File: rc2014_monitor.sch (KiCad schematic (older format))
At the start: 25 parts, among them J1 Z80 Bus, J2 Pro Bus, J3 USB_B_Micro, J4 M3 Mounting Hole, SW2 SW_Push, U3 74HCT541, U4 74HCT541, U5 74HCT541, U7 MAX40200AUK, U8 MAX40200AUK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

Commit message: trace cleanup
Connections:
- net labels added: CLK
- wire segments 99 -> 101
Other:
- moved on the sheet: C3, C4, C5, J4, U3, U4, U5

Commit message: use reset to clear the displays
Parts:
- added U11: 74HCT00, Package_DIP:DIP-14_W7.62mm, symbol 74xx:74HCT00
- U9: footprint Package_TO_SOT_SMD:SOT-23 -> Package_TO_SOT_SMD:SOT-23_Handsoldering
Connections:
- net labels added: CLR, RN2_2
- wire segments 101 -> 107
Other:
- note added: "Reset Monitor & Display Blank"
- note removed: "Reset Monitor"
- moved on the sheet: C10, C3, C4, C5, JP5, SW2, U3, U4, U5, U9

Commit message: Fixed some courtyard overlaps and rotary switch orientation
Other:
- moved on the sheet: C7, C8, C9, J3, U7, U8

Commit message: changes to stepper circuit, pcb layout changes
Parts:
- DISP0, DISP1, DISP2, DISP3, DISP4, DISP5: symbol rc2014_monitor-rescue:TIL311-Display_Character -> rc2014_monitor-rescue:TIL311
- renumbered C7 to C17, C9 to C7, C10 to C9, U3 to U1, U4 to U2, U5 to U3
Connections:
- net labels added: RESET, RN2_1
- net labels removed: CLR, RN2_2
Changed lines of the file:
@@
 $EndDescr
 $Comp
-L rc2014_monitor-rescue:TIL311-Display_Character DISP5
+L rc2014_monitor-rescue:TIL311 DISP5
 U 1 1 5CB4BA92
 P 2000 1500
@@
 $EndComp
 $Comp
-L rc2014_monitor-rescue:TIL311-Display_Character DISP4
+L rc2014_monitor-rescue:TIL311 DISP4
 U 1 1 5CB4CB07
 P 3550 1500
@@
 $EndComp
 $Comp
-L rc2014_monitor-rescue:TIL311-Display_Character DISP3
+L rc2014_monitor-rescue:TIL311 DISP3
 U 1 1 5CB4D9E8
 P 5100 1500
@@
 $EndComp
 $Comp
-L rc2014_monitor-rescue:TIL311-Display_Character DISP2
+L rc2014_monitor-rescue:TIL311 DISP2
 U 1 1 5CB570C9
 P 6650 1500
@@
 $EndComp
 $Comp
-L rc2014_monitor-rescue:TIL311-Display_Character DISP0
+L rc2014_monitor-rescue:TIL311 DISP0
 U 1 1 5CB570D5
 P 9800 1500
@@
 $EndComp
 $Comp
-L rc2014_monitor-rescue:TIL311-Display_Character DISP1
+L rc2014_monitor-rescue:TIL311 DISP1
 U 1 1 5CB570CF
 P 8150 1500
@@
 $EndComp
 $Comp
-L Device:C C7
+L Device:C C17
 U 1 1 5CB2CAB8
 P 4250 6350
-F 0 "C7" H 4365 6396 50  0000 L CNN
+F 0 "C17" H 4365 6396 50  0000 L CNN
 F 1 "100nF" H 4365 6305 50  0000 L CNN
 F 2 "Capacitor_SMD:C_0805_2012Metric_Pad1.15x1.40mm_HandSolder" H 4288 6200 50  0001 C CNN
@@
 	5850 7150 2350 7150
 $Sheet
-S 6250 2850 1200 800
+S 9000 2750 1200 800
 U 5CBDBC11
 F0 "LatchSelector" 50
@@
 ~RESET
 $Comp
-L Device:C C10
+L Device:C C9
 U 1 1 5CB1BEC1
 P 3850 4700
-F 0 "C10" H 3965 4746 50  0000 L CNN
+F 0 "C9" H 3965 4746 50  0000 L CNN
 F 1 "100nF" H 3965 4655 50  0000 L CNN
 F 2 "Capacitor_SMD:C_0805_2012Metric_Pad1.15x1.40mm_HandSolder" H 3888 4550 50  0001 C CNN
@@
 	6100 5300 6100 5600
 $Comp
-L 74xx:74HCT541 U3
+L 74xx:74HCT541 U1
 U 1 1 5CB94EBF
 P 6600 4800
-F 0 "U3" H 6400 5450 50  0000 C CNN
+F 0 "U1" H 6400 5450 50  0000 C CNN
 F 1 "74HCT541" H 6600 4500 50  0000 C CNN
 F 2 "Package_DIP:DIP-20_W7.62mm" H 6600 4800 50  0001 C CNN
@@
 Connection ~ 6100 5300
 $Comp
-L 74xx:74HCT541 U4
+L 74xx:74HCT541 U2
 U 1 1 5CBBA2FE
 P 8500 4800
-F 0 "U4" H 8300 5450 50  0000 C CNN
+F 0 "U2" H 8300 5450 50  0000 C CNN
 F 1 "74HCT541" H 8500 4500 50  0000 C CNN
 F 2 "Package_DIP:DIP-20_W7.62mm" H 8500 4800 50  0001 C CNN
@@
 $EndComp
 $Comp
-L 74xx:74HCT541 U5
+L 74xx:74HCT541 U3
 U 1 1 5CBBDA4F
 P 10400 4800
-F 0 "U5" H 10200 5450 50  0000 C CNN
+F 0 "U3" H 10200 5450 50  0000 C CNN
 F 1 "74HCT541" H 10400 4500 50  0000 C CNN
 F 2 "Package_DIP:DIP-20_W7.62mm" H 10400 4800 50  0001 C CNN
@@
 	3550 6600 4000 6600
 $Comp
-L Device:C C9
+L Device:C C7
 U 1 1 5CCF3BD8
 P 4000 6350
-F 0 "C9" H 4115 6396 50  0000 L CNN
+F 0 "C7" H 4115 6396 50  0000 L CNN
 F 1 "1uF" H 4115 6305 50  0000 L CNN
 F 2 "Capacitor_SMD:C_0805_2012Metric_Pad1.15x1.40mm_HandSolder" H 4038 6200 50  0001 C CNN
@@
 $Comp
 L 74xx:74HCT00 U?
-U 4 1 5CBA6ACE
+U 3 1 5CBA6ACE
 P 4650 3950
 AR Path="/5CBDBC11/5CBA6ACE" Ref="U?"  Part="4"
-AR Path="/5CBA6ACE" Ref="U11"  Part="4"
+AR Path="/5CBA6ACE" Ref="U11"  Part="3"
 F 0 "U11" H 4650 4275 50  0000 C CNN
 F 1 "74HCT00" H 4650 4184 50  0000 C CNN
@@
 F 7 "Mouser" H 2900 -1900 50  0001 C CNN "SPR"
 F 8 "https://www.mouser.com/ProductDetail/Texas-Instruments/CD74HCT00E?qs=%2Fha2pyFadui%2FKTy9HJ5lB2bvnS2yYlFmKLu9w5G%252BX5xMG4CMjJrhdg%3D%3D" H 2900 -1900 50  0001 C CNN "SPURL"
-	4    4650 3950
+	3    4650 3950
 	1    0    0    -1
 $EndComp
@@
 	4350 3950 4350 4050
 Text GLabel 4200 3650 1    50   Input ~ 0
-RN2_2
+RN2_1
 Wire Wire Line
 	4200 3650 4200 3950
@@
 Connection ~ 4200 3950
 Text GLabel 4950 3950 2    50   Output ~ 0
-CLR
+RESET
 Wire Wire Line
 	2000 2200 3550 2200
@@
 Connection ~ 4500 2500
 Wire Wire Line
-	4500 2500 5350 2500
-Wire Wire Line
 	2950 1900 2950 2500
 Connection ~ 2950 2500
 Wire Wire Line
 	2950 2500 4500 2500
-Text GLabel 5350 2700 3    50   Input ~ 0
-CLR
+Text GLabel 5350 2600 3    50   Input ~ 0
+RESET
 Wire Wire Line
 	5900 2400 4350 2400
-Wire Wire Line
-	5350 2700 5350 2500
-Connection ~ 5350 2500
-Wire Wire Line
-	5350 2500 6050 2500
 Wire Notes Line
 	5250 3300 5250 5250
 Wire Notes Line
 	2350 3300 2350 5250
+Wire Wire Line
+	4500 2500 5350 2500
+Wire Wire Line
+	5350 2600 5350 2500
+Connection ~ 5350 2500
+Wire Wire Line
+	5350 2500 6050 2500
 $EndSCHEMATC

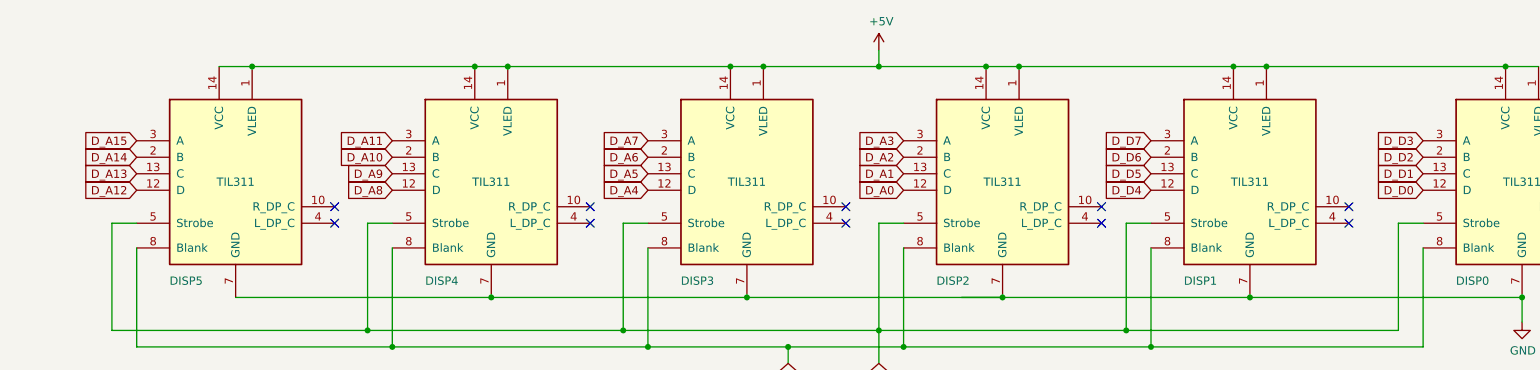
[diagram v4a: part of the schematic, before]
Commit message: fixed single step, display hookup
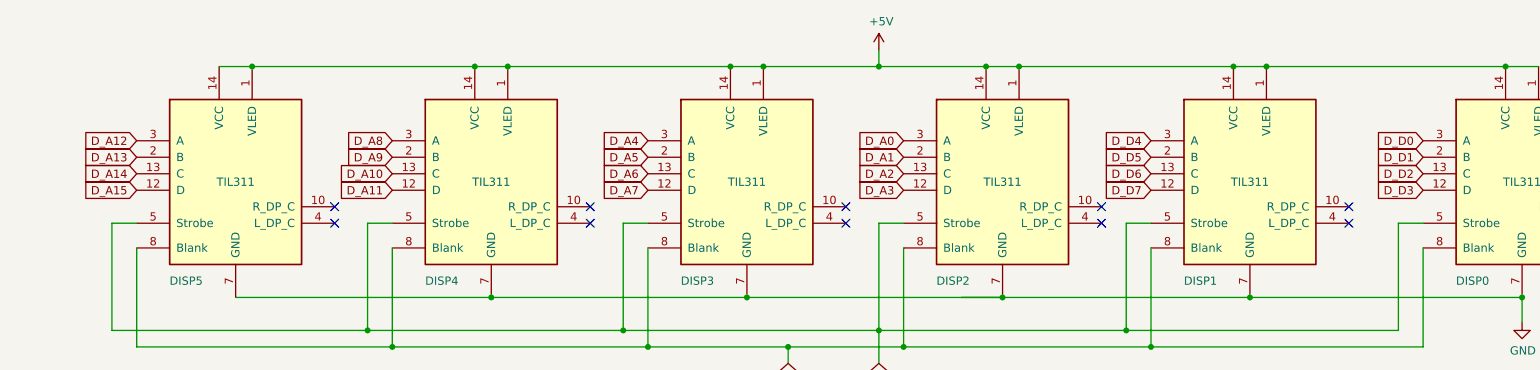
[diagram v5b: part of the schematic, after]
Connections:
- net D_A0: now also DISP2.3 (A); no longer DISP2.12 (D)
- net D_A1: now also DISP2.2 (B); no longer DISP2.13 (C)
- net D_A10: now also DISP4.13 (C); no longer DISP4.2 (B)
- net D_A11: now also DISP4.12 (D); no longer DISP4.3 (A)
- net D_A12: now also DISP5.3 (A); no longer DISP5.12 (D)
- net D_A13: now also DISP5.2 (B); no longer DISP5.13 (C)
- net D_A14: now also DISP5.13 (C); no longer DISP5.2 (B)
- net D_A15: now also DISP5.12 (D); no longer DISP5.3 (A)
- net D_A2: now also DISP2.13 (C); no longer DISP2.2 (B)
- net D_A3: now also DISP2.12 (D); no longer DISP2.3 (A)
- net D_A4: now also DISP3.3 (A); no longer DISP3.12 (D)
- net D_A5: now also DISP3.2 (B); no longer DISP3.13 (C)
- net D_A6: now also DISP3.13 (C); no longer DISP3.2 (B)
- net D_A7: now also DISP3.12 (D); no longer DISP3.3 (A)
- net D_A8: now also DISP4.3 (A); no longer DISP4.12 (D)
- net D_A9: now also DISP4.2 (B); no longer DISP4.13 (C)
- net D_D0: now also DISP0.3 (A); no longer DISP0.12 (D)
- net D_D1: now also DISP0.2 (B); no longer DISP0.13 (C)
- net D_D2: now also DISP0.13 (C); no longer DISP0.2 (B)
- net D_D3: now also DISP0.12 (D); no longer DISP0.3 (A)
- net D_D4: now also DISP1.3 (A); no longer DISP1.12 (D)
- net D_D5: now also DISP1.2 (B); no longer DISP1.13 (C)
- net D_D6: now also DISP1.13 (C); no longer DISP1.2 (B)
- net D_D7: now also DISP1.12 (D); no longer DISP1.3 (A)
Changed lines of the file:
@@
 Text GLabel 5600 6200 2    50   Input ~ 0
 5V
+Text GLabel 1400 1550 0    50   Input ~ 0
+D_A15
+Text GLabel 1400 1450 0    50   Input ~ 0
+D_A14
+Text GLabel 1400 1350 0    50   Input ~ 0
+D_A13
 Text GLabel 1400 1250 0    50   Input ~ 0
-D_A15
-Text GLabel 1400 1350 0    50   Input ~ 0
-D_A14
-Text GLabel 1400 1450 0    50   Input ~ 0
-D_A13
-Text GLabel 1400 1550 0    50   Input ~ 0
 D_A12
+Text GLabel 2950 1450 0    50   Input ~ 0
+D_A10
 Text GLabel 2950 1350 0    50   Input ~ 0
-D_A10
-Text GLabel 2950 1450 0    50   Input ~ 0
 D_A9
+Text GLabel 2950 1250 0    50   Input ~ 0
+D_A8
 Text GLabel 2950 1550 0    50   Input ~ 0
-D_A8
-Text GLabel 2950 1250 0    50   Input ~ 0
 D_A11
 Text GLabel 5900 2600 3    50   Input ~ 0
 LATCH
+Text GLabel 6050 1550 0    50   Input ~ 0
+D_A3
+Text GLabel 6050 1450 0    50   Input ~ 0
+D_A2
+Text GLabel 6050 1350 0    50   Input ~ 0
+D_A1
 Text GLabel 6050 1250 0    50   Input ~ 0
-D_A3
-Text GLabel 6050 1350 0    50   Input ~ 0
-D_A2
-Text GLabel 6050 1450 0    50   Input ~ 0
-D_A1
-Text GLabel 6050 1550 0    50   Input ~ 0
 D_A0
+Text GLabel 4500 1550 0    50   Input ~ 0
+D_A7
+Text GLabel 4500 1450 0    50   Input ~ 0
+D_A6
+Text GLabel 4500 1350 0    50   Input ~ 0
+D_A5
 Text GLabel 4500 1250 0    50   Input ~ 0
-D_A7
-Text GLabel 4500 1350 0    50   Input ~ 0
-D_A6
-Text GLabel 4500 1450 0    50   Input ~ 0
-D_A5
-Text GLabel 4500 1550 0    50   Input ~ 0
 D_A4
-Text GLabel 9200 1250 0    50   Input ~ 0
+Text GLabel 9200 1550 0    50   Input ~ 0
 D_D3
+Text GLabel 9200 1450 0    50   Input ~ 0
+D_D2
 Text GLabel 9200 1350 0    50   Input ~ 0
-D_D2
-Text GLabel 9200 1450 0    50   Input ~ 0
 D_D1
-Text GLabel 9200 1550 0    50   Input ~ 0
-D_D0
+Text GLabel 7550 1550 0    50   Input ~ 0
+D_D7
+Text GLabel 7550 1450 0    50   Input ~ 0
+D_D6
+Text GLabel 7550 1350 0    50   Input ~ 0
+D_D5
 Text GLabel 7550 1250 0    50   Input ~ 0
-D_D7
-Text GLabel 7550 1350 0    50   Input ~ 0
-D_D6
-Text GLabel 7550 1450 0    50   Input ~ 0
-D_D5
-Text GLabel 7550 1550 0    50   Input ~ 0
 D_D4
 Text GLabel 10900 4500 2    50   Output ~ 0
@@
 Wire Wire Line
 	5350 2500 6050 2500
+Text GLabel 9200 1250 0    50   Input ~ 0
+D_D0
 $EndSCHEMATC

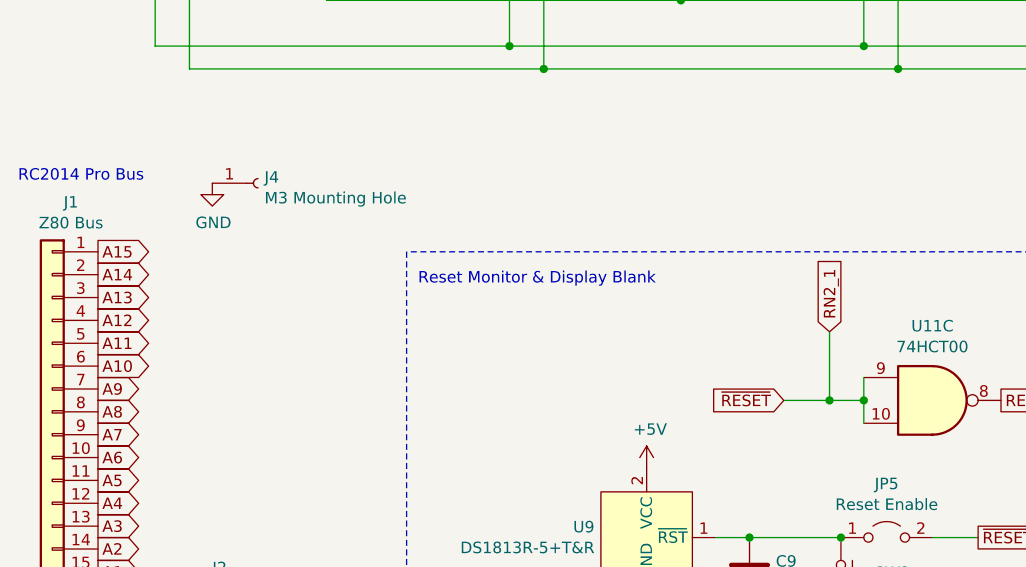
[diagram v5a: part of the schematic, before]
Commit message: Reorganized board yet again, replaced SMD 555 with TH
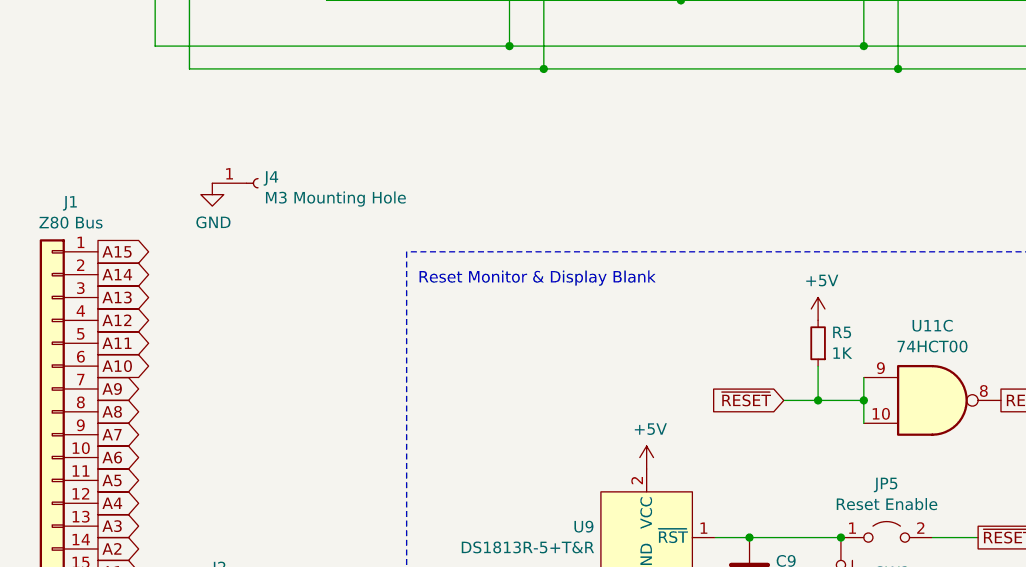
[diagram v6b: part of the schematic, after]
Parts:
- added R5: 1K, Resistor_SMD:R_0805_2012Metric_Pad1.15x1.40mm_HandSolder, symbol Device:R_Small
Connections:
- net +5V: now also R5.2
- net RN2_1 renamed ~RESET
- net ~RESET: now also R5.1
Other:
- note removed: "RC2014 Pro Bus"
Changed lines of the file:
@@
-$EndComp
-$Comp
-L power:GND #PWR0114
-U 1 1 5CB5974C
-P 2650 6900
-AR Path="/5CB5974C" Ref="#PWR0114"  Part="1"
-AR Path="/5CB63856/5CB5974C" Ref="#PWR?"  Part="1"
-AR Path="/5CB5AB00/5CB63856/5CB5974C" Ref="#PWR?"  Part="1"
-F 0 "#PWR0114" H 2650 6650 50  0001 C CNN
-F 1 "GND" H 2655 6727 50  0000 C CNN
-F 2 "" H 2650 6900 50  0001 C CNN
-F 3 "" H 2650 6900 50  0001 C CNN
-	1    2650 6900
-	1    0    0    -1
-$EndComp
-$Comp
-L Connector:USB_B_Micro J3
-U 1 1 5CAA0A65
-P 2650 6400
-F 0 "J3" H 2707 6867 50  0000 C CNN
-F 1 "USB_B_Micro" H 2707 6776 50  0000 C CNN
-F 2 "Connector_USB:USB_Micro-B_Amphenol_10103594-0001LF_Horizontal" H 2800 6350 50  0001 C CNN
-F 3 "https://www.mouser.com/datasheet/2/18/10103594-1361315.pdf" H 2800 6350 50  0001 C CNN
-F 4 "Amphenol" H -6300 800 50  0001 C CNN "MFR"
-F 5 "10103594-0001LF" H -6300 800 50  0001 C CNN "MPN"
-F 6 "Mouser" H -6300 800 50  0001 C CNN "SPR"
-F 7 "649-10103594-0001LF" H -6300 800 50  0001 C CNN "SPN"
-F 8 "https://www.mouser.com/ProductDetail/Amphenol-FCI/10103594-0001LF?qs=%2Fha2pyFadui3tF6%252BEBESQPkzCvC45QB71td3CV1bdDjkgdfJGIcfa4Qftb3SNhsX" H -6300 800 50  0001 C CNN "SPURL"
-	1    2650 6400
-	1    0    0    -1
 $EndComp
 $Comp
@@
 Text GLabel 1000 3800 2    50   Output ~ 0
 A10
-Text Notes 650  3000 0    50   ~ 0
-RC2014 Pro Bus
 Text GLabel 6100 4700 0    50   Input ~ 0
 A11
@@
 	9800 2350 9800 2200
 Wire Wire Line
-	2650 6800 2650 6850
-Wire Wire Line
-	2550 6800 2550 6850
-Wire Wire Line
-	2550 6850 2650 6850
-Wire Wire Line
-	2650 6850 2650 6900
-Wire Wire Line
 	5900 800  6550 800
 Wire Wire Line
@@
 Connection ~ 3450 800
 Connection ~ 9800 2200
-Connection ~ 2650 6850
 Connection ~ 5900 800
 Connection ~ 6600 6050
@@
 NoConn ~ 1000 6700
 NoConn ~ 1000 6800
-NoConn ~ 2950 6400
-NoConn ~ 2950 6500
-NoConn ~ 2950 6600
 $Comp
 L Analog_Switch:MAX40200AUK U7
@@
 Wire Wire Line
 	5500 6200 5600 6200
-Wire Wire Line
-	2950 6200 3150 6200
-Connection ~ 3150 6200
 Wire Wire Line
 	4250 6500 4250 6600
@@
 Wire Notes Line
 	2350 5250 5250 5250
-Wire Notes Line
-	5250 3300 2350 3300
 Text Notes 2400 3450 0    50   ~ 0
 Reset Monitor & Display Blank
@@
 Wire Wire Line
 	4350 3850 4350 3950
-Wire Wire Line
-	4000 3950 4200 3950
 Connection ~ 4350 3950
 Wire Wire Line
 	4350 3950 4350 4050
-Text GLabel 4200 3650 1    50   Input ~ 0
-RN2_1
-Wire Wire Line
-	4200 3650 4200 3950
-Wire Wire Line
-	4200 3950 4350 3950
-Connection ~ 4200 3950
 Text GLabel 4950 3950 2    50   Output ~ 0
 RESET
@@
 Text GLabel 9200 1250 0    50   Input ~ 0
 D_D0
+Wire Notes Line
+	5250 3300 2350 3300
+Wire Wire Line
+	4000 3950 4150 3950
+$Comp
+L Device:R_Small R?
+U 1 1 5CC78D11
+P 4150 3700
+AR Path="/5CBDBC11/5CC78D11" Ref="R?"  Part="1"
+AR Path="/5CC78D11" Ref="R5"  Part="1"
+F 0 "R5" H 4091 3654 50  0000 R CNN
+F 1 "1K" H 4091 3745 50  0000 R CNN
+F 2 "Resistor_SMD:R_0805_2012Metric_Pad1.15x1.40mm_HandSolder" H 4150 3700 50  0001 C CNN
+F 3 "~" H 4150 3700 50  0001 C CNN
+	1    4150 3700
+	-1   0    0    1
+$EndComp
+$Comp
+L power:+5V #PWR0133
+U 1 1 5CC78D17
+P 4150 3600
+AR Path="/5CC78D17" Ref="#PWR0133"  Part="1"
+AR Path="/5CB63856/5CC78D17" Ref="#PWR?"  Part="1"
+AR Path="/5CB5AB00/5CB63856/5CC78D17" Ref="#PWR?"  Part="1"
+AR Path="/5CBDBC11/5CC78D17" Ref="#PWR?"  Part="1"
+F 0 "#PWR0133" H 4150 3450 50  0001 C CNN
+F 1 "+5V" H 4165 3773 50  0000 C CNN
+F 2 "" H 4150 3600 50  0001 C CNN
+F 3 "" H 4150 3600 50  0001 C CNN
+	1    4150 3600
+	1    0    0    -1
+$EndComp
+Wire Wire Line
+	4150 3800 4150 3950
+Connection ~ 4150 3950
+Wire Wire Line
+	4150 3950 4350 3950
+Connection ~ 3150 6200
+Wire Wire Line
+	2950 6200 3150 6200
+NoConn ~ 2950 6600
+NoConn ~ 2950 6500
+NoConn ~ 2950 6400
+Wire Wire Line
+	2650 6850 2650 6900
+Wire Wire Line
+	2550 6850 2650 6850
+Wire Wire Line
+	2550 6800 2550 6850
+Connection ~ 2650 6850
+Wire Wire Line
+	2650 6800 2650 6850
+$Comp
+L Connector:USB_B_Micro J3
+U 1 1 5CAA0A65
+P 2650 6400
+F 0 "J3" H 2707 6867 50  0000 C CNN
+F 1 "USB_B_Micro" H 2707 6776 50  0000 C CNN
+F 2 "Connector_USB:USB_Micro-B_Amphenol_10103594-0001LF_Horizontal" H 2800 6350 50  0001 C CNN
+F 3 "https://www.mouser.com/datasheet/2/18/10103594-1361315.pdf" H 2800 6350 50  0001 C CNN
+F 4 "Amphenol" H -6300 800 50  0001 C CNN "MFR"
+F 5 "10103594-0001LF" H -6300 800 50  0001 C CNN "MPN"
+F 6 "Mouser" H -6300 800 50  0001 C CNN "SPR"
+F 7 "649-10103594-0001LF" H -6300 800 50  0001 C CNN "SPN"
+F 8 "https://www.mouser.com/ProductDetail/Amphenol-FCI/10103594-0001LF?qs=%2Fha2pyFadui3tF6%252BEBESQPkzCvC45QB71td3CV1bdDjkgdfJGIcfa4Qftb3SNhsX" H -6300 800 50  0001 C CNN "SPURL"
+	1    2650 6400
+	1    0    0    -1
+$EndComp
+$Comp
+L power:GND #PWR0114
+U 1 1 5CB5974C
+P 2650 6900
+AR Path="/5CB5974C" Ref="#PWR0114"  Part="1"
+AR Path="/5CB63856/5CB5974C" Ref="#PWR?"  Part="1"
+AR Path="/5CB5AB00/5CB63856/5CB5974C" Ref="#PWR?"  Part="1"
+F 0 "#PWR0114" H 2650 6650 50  0001 C CNN
+F 1 "GND" H 2655 6727 50  0000 C CNN
+F 2 "" H 2650 6900 50  0001 C CNN
+F 3 "" H 2650 6900 50  0001 C CNN
+	1    2650 6900
+	1    0    0    -1
+$EndComp
 $EndSCHEMATC

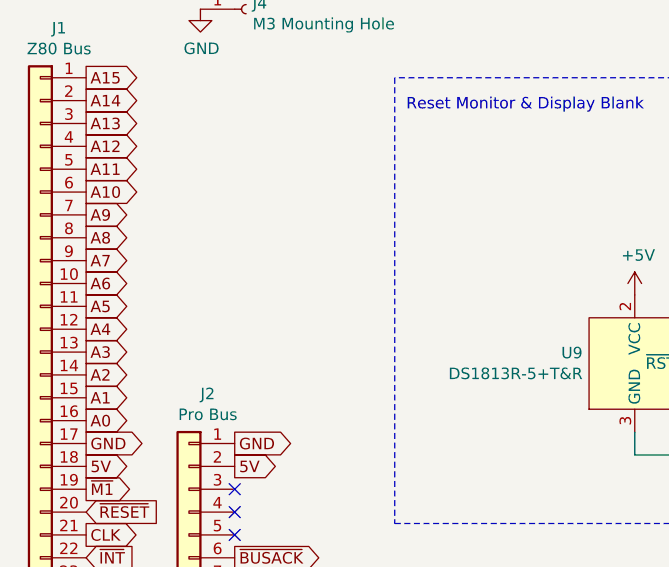
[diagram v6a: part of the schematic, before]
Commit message: more routing changes
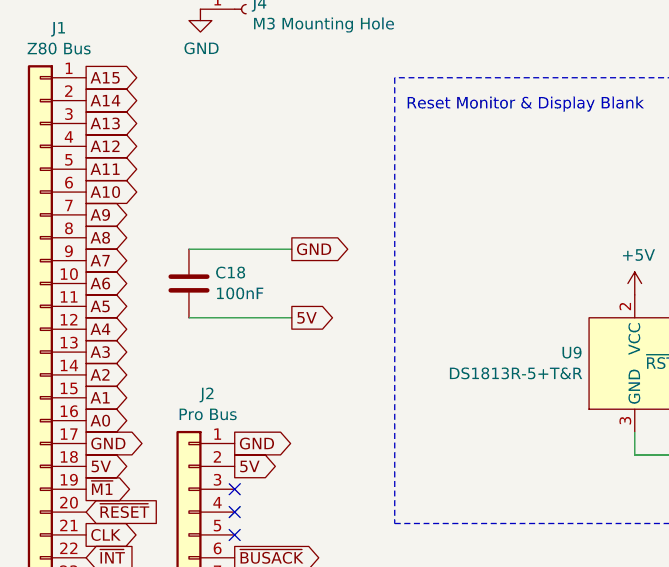
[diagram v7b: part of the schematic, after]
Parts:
- added C18: 100nF, Capacitor_SMD:C_0805_2012Metric_Pad1.15x1.40mm_HandSolder, symbol Device:C
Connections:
- net 5V: now also C18.2
- net GND: now also C18.1
